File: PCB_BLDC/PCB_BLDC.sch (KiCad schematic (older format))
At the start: 70 parts, among them J1 Conn_01x01_Female, J10 Conn_01x06, J11 Conn_01x08, J12 Conn_01x06, J13 Conn_01x08, J14 Conn_01x08, J15 Conn_01x10, J16 Conn_01x08, J17 Conn_01x10, J2 Conn_01x01_Female, J3 Conn_01x01_Female, J4 Conn_01x01_Female, J5 Conn_01x01_Female, J6 Conn_01x01_Female, J7 Conn_01x01_Female, J8 VCC_Unregulated, J9 VCC_GND, Q1 IRF4905, SW1 Rotary_Encoder, U1 MagI3C WPMDH1100XX1S / 173010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, U2 BTN8962TA, U3 BTN8962TA, U4 BTN8962TA

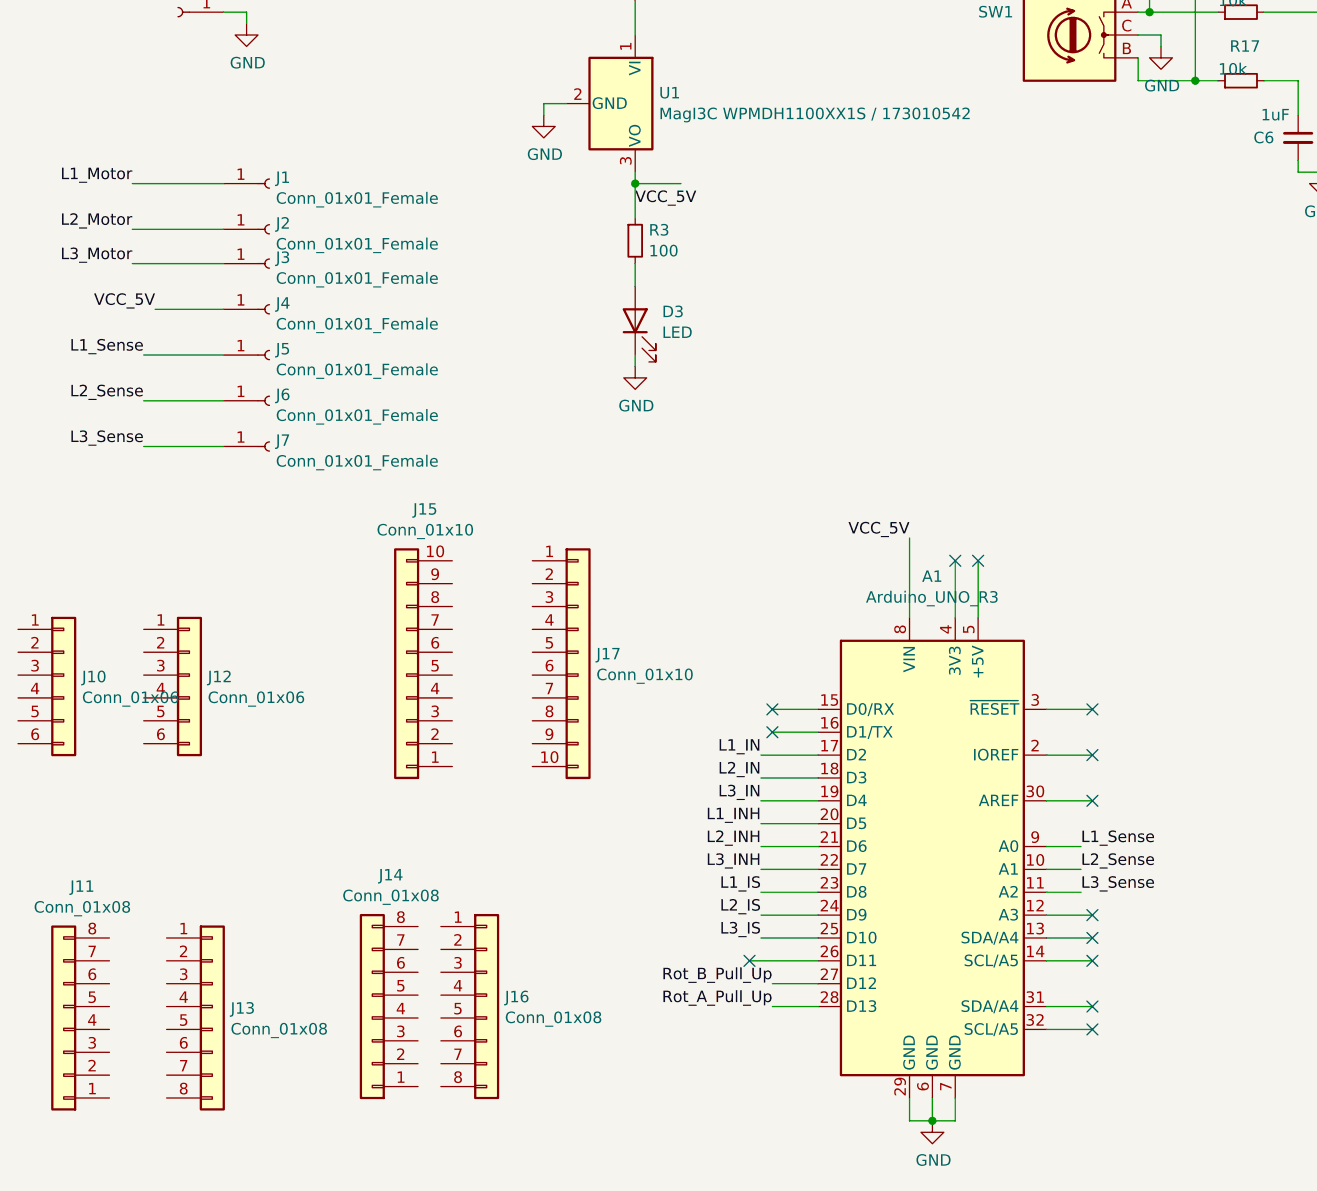
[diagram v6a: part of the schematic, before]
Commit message: Main: Update Arduino Pins, PCB Routing
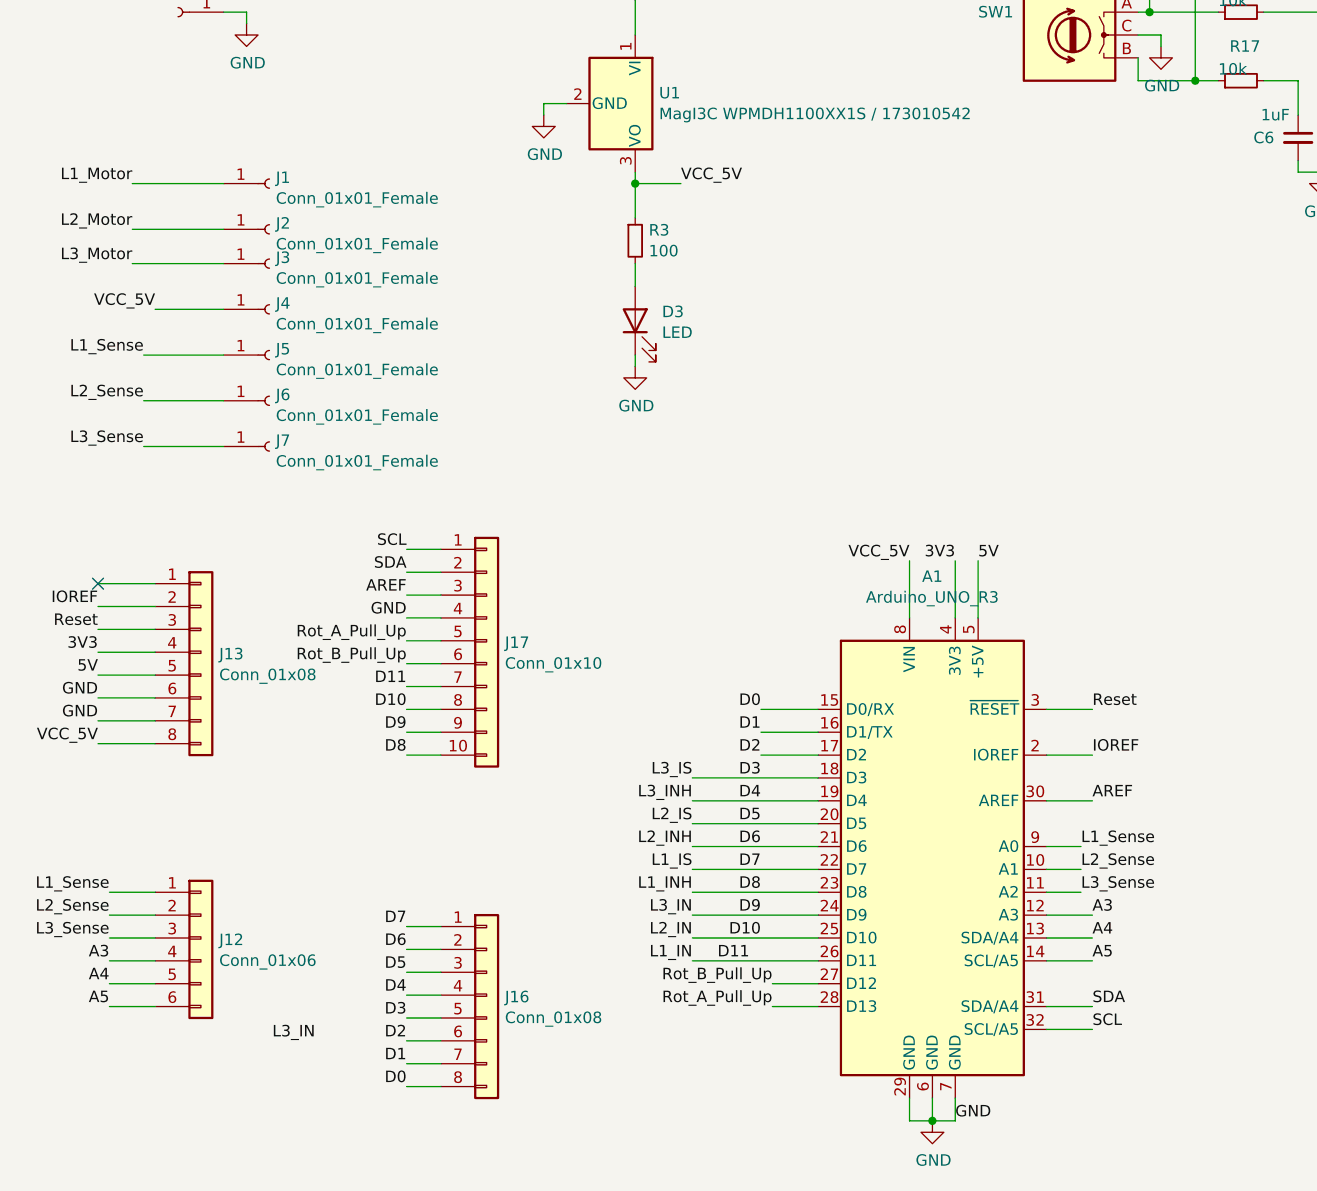
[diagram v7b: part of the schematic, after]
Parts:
- removed J10: Conn_01x06, Connector_PinHeader_2.54mm:PinHeader_1x06_P2.54mm_Vertical, symbol Connector_Generic:Conn_01x06
- removed J11, J14: Conn_01x08, Connector_PinHeader_2.54mm:PinHeader_1x08_P2.54mm_Vertical, symbol Connector_Generic:Conn_01x08
- removed J15: Conn_01x10, Connector_PinHeader_2.54mm:PinHeader_1x10_P2.54mm_Vertical, symbol Connector_Generic:Conn_01x10
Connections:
- net L2_INH is gone; now on net D6: A1.21 (D6), R11.2
- net GND: now also J13.6 (Pin_6), J13.7 (Pin_7), J17.4 (Pin_4)
- net L1_Sense: now also J12.1 (Pin_1)
- net L2_Sense: now also J12.2 (Pin_2)
- net L3_Sense: now also J12.3 (Pin_3)
- net Rot_A_Pull_Up: now also J17.5 (Pin_5)
- net Rot_B_Pull_Up: now also J17.6 (Pin_6)
- net VCC_5V: now also J13.8 (Pin_8)
- net A3: now reaches A1.12 (A3)
- net A3: now also J12.4 (Pin_4)
- net A4: now reaches A1.13 (SDA/A4)
- net A4: now also J12.5 (Pin_5)
- net A5: now reaches A1.14 (SCL/A5)
- net A5: now also J12.6 (Pin_6)
- net D0: now reaches A1.15 (D0/RX)
- net D0: now also J16.8 (Pin_8)
- net D1: now reaches A1.16 (D1/TX)
- net D1: now also J16.7 (Pin_7)
- net IOREF: now reaches A1.2 (IOREF)
- net IOREF: now also J13.2 (Pin_2)
- net D11: now reaches A1.26 (D11)
- net D11: now also J17.7 (Pin_7), R9.2
- net Reset: now reaches A1.3 (~RESET)
- net Reset: now also J13.3 (Pin_3)
- net AREF: now reaches A1.30 (AREF)
- net AREF: now also J17.3 (Pin_3)
- net SDA: now reaches A1.31 (SDA/A4)
- net SDA: now also J17.2 (Pin_2)
- net SCL: now reaches A1.32 (SCL/A5)
- net SCL: now also J17.1 (Pin_1)
- net 3V3: now reaches A1.4 (3V3)
- net 3V3: now also J13.4 (Pin_4)
- net 5V: now reaches A1.5 (+5V)
- net 5V: now also J13.5 (Pin_5)
- net D8: now reaches J17.10 (Pin_10)
- net D8: now also A1.23 (D8), R8.2
- net D10: now reaches J17.8 (Pin_8)
- net D10: now also A1.25 (D10), R12.2
- net D9: now reaches J17.9 (Pin_9)
- net D9: now also A1.24 (D9), R15.2
- net D7: now reaches J16.1 (Pin_1)
- net D7: now also A1.22 (D7), C8.1, R4.2, U2.6 (IS)
- net D6: now reaches J16.2 (Pin_2)
- net D5: now reaches J16.3 (Pin_3)
- net D5: now also A1.20 (D5), C9.1, R5.2, U3.6 (IS)
- net D4: now reaches J16.4 (Pin_4)
- net D4: now also A1.19 (D4), R14.2
- net D3: now reaches J16.5 (Pin_5)
- net D3: now also A1.18 (D3), C10.1, R6.2, U4.6 (IS)
- net D2: now reaches J16.6 (Pin_6)
- net D2: now also A1.17 (D2)
- removed net L1_IN: A1.17 (D2), R9.2
- removed net L1_INH: A1.20 (D5), R8.2
- removed net L1_IS: A1.23 (D8), C8.1, R4.2, U2.6 (IS)
- removed net L2_IN: A1.18 (D3), R12.2
- removed net L2_IS: A1.24 (D9), C9.1, R5.2, U3.6 (IS)
- removed net L3_IN: A1.19 (D4), R15.2
- removed net L3_INH: A1.22 (D7), R14.2
- removed net L3_IS: A1.25 (D10), C10.1, R6.2, U4.6 (IS)
- no-connect marks 13 -> 1
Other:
- moved on the sheet: J12, J13, J17

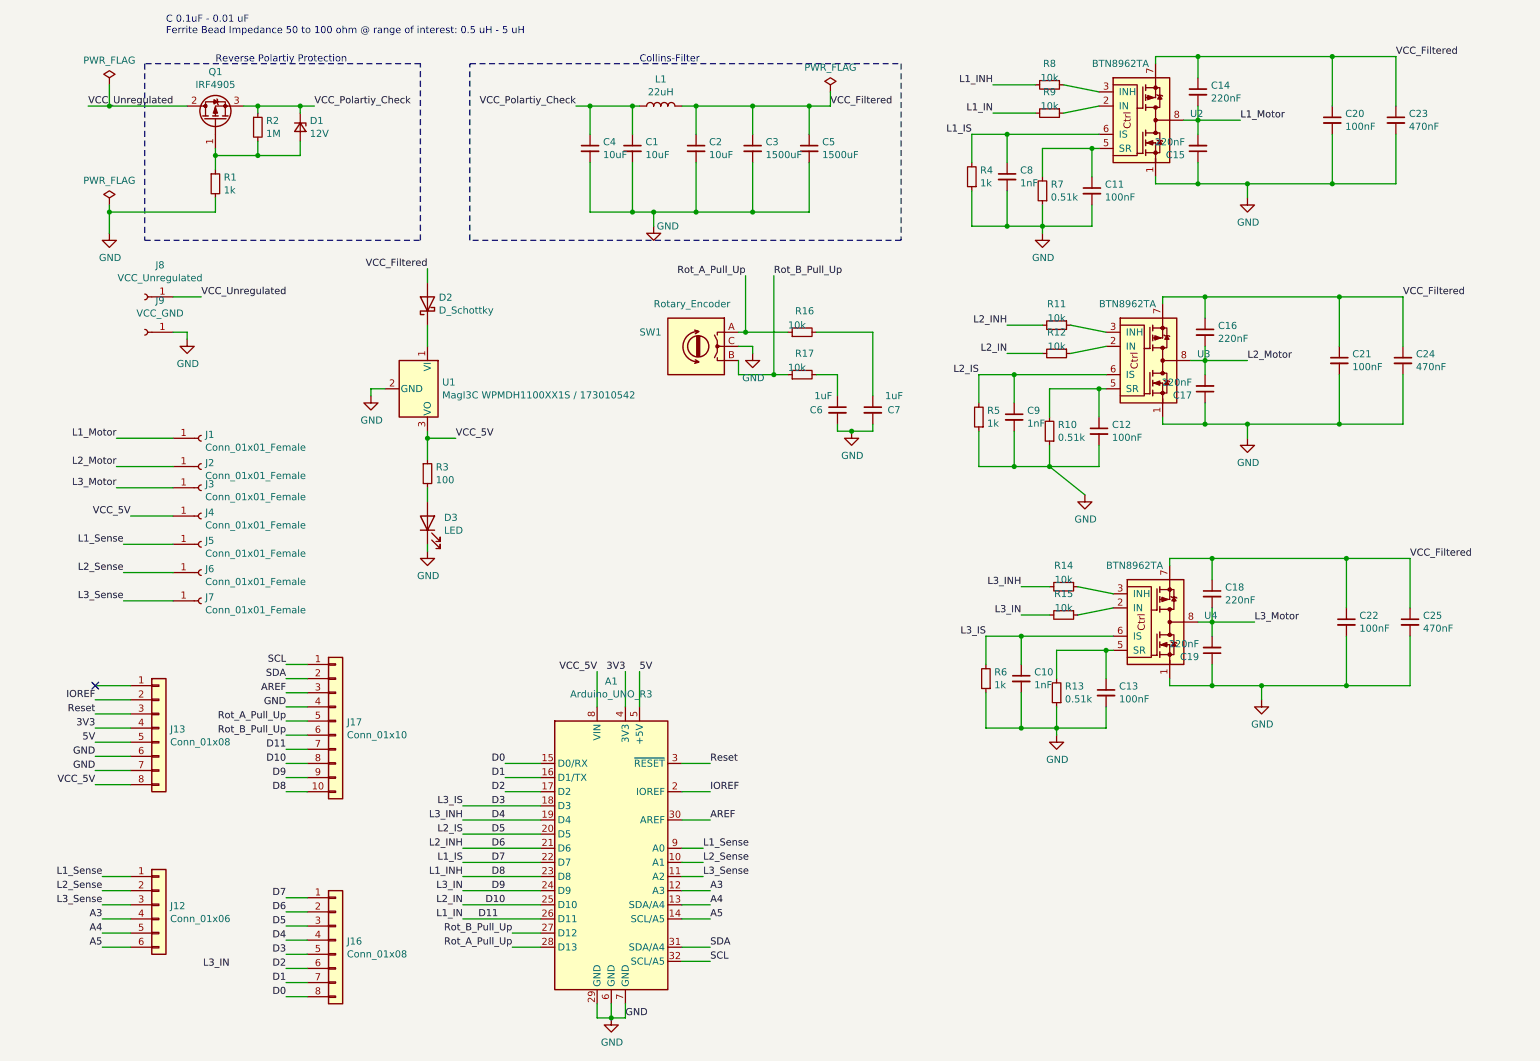
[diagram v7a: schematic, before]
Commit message: Main: Update Routing, Schmematic to use Analog Ports of Arduino
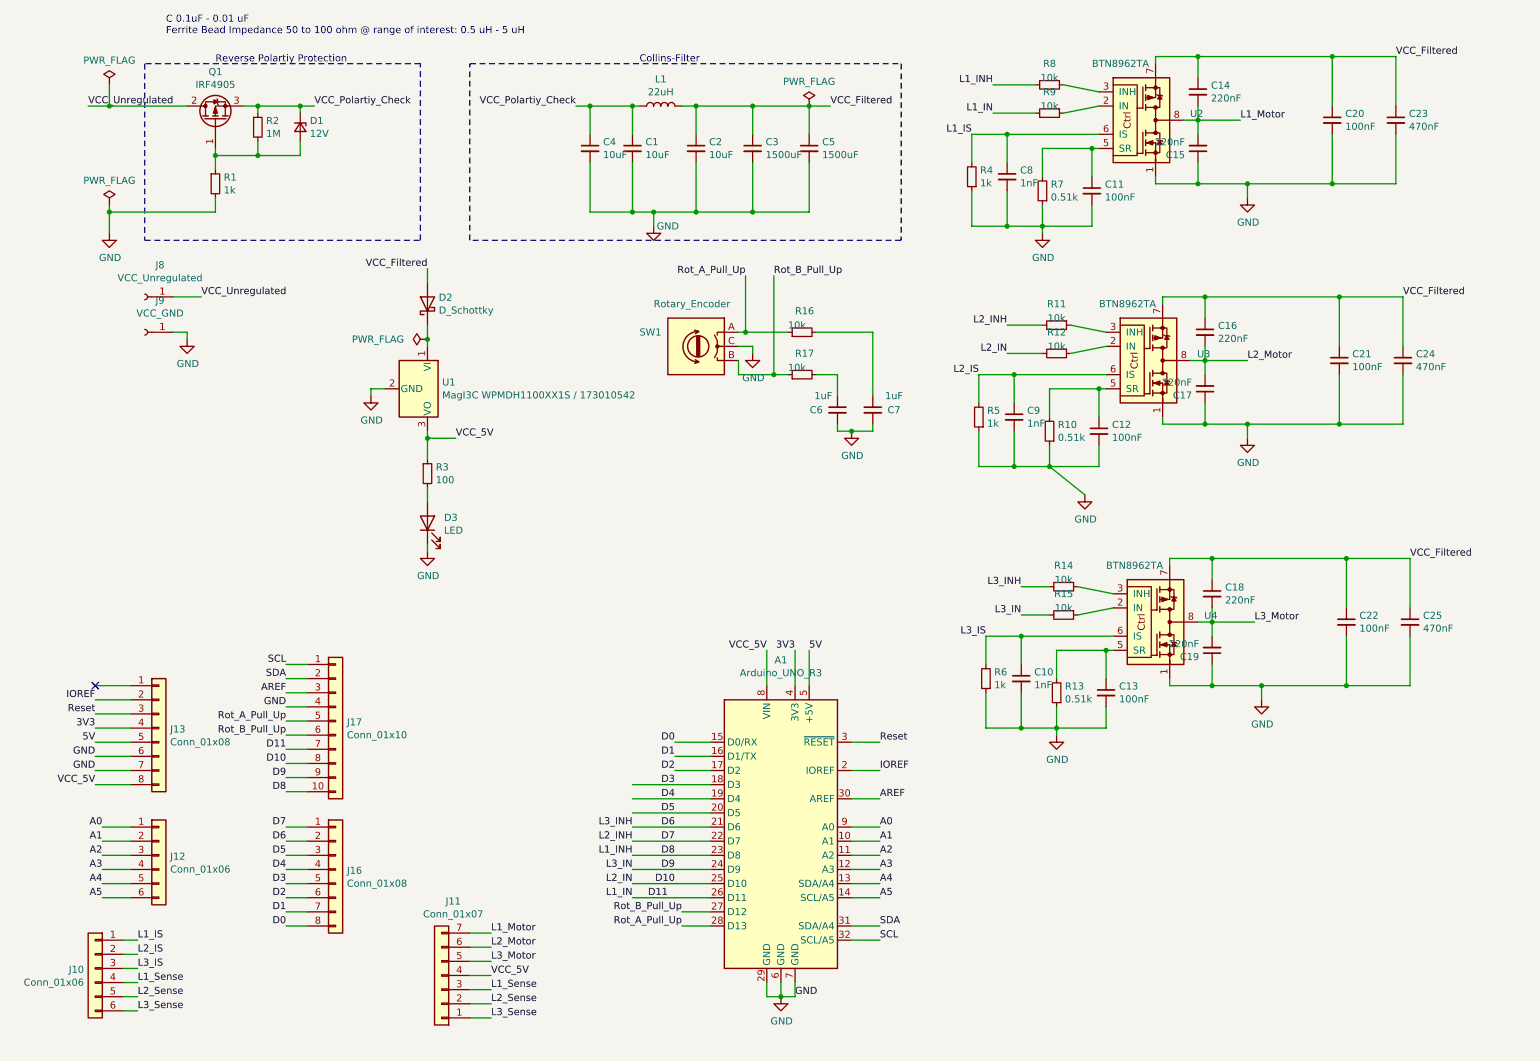
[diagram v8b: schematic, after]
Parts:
- removed J1, J2, J3, J4, J5, J6, J7: Conn_01x01_Female, Connector_Pin:Pin_D1.0mm_L10.0mm, symbol Connector:Conn_01x01_Female
- added J10: Conn_01x06, Connector_PinSocket_2.54mm:PinSocket_1x06_P2.54mm_Vertical, symbol Connector_Generic:Conn_01x06
- added J11: Conn_01x07, TerminalBlock_Phoenix:TerminalBlock_Phoenix_MKDS-1,5-7_1x07_P5.00mm_Horizontal, symbol Connector_Generic:Conn_01x07
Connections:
- net D3: no longer C10.1, R6.2, U4.6 (IS)
- net D4: no longer R14.2
- net D5: no longer C9.1, R5.2, U3.6 (IS)
- net D6: now also R14.2; no longer R11.2
- net D7: now also R11.2; no longer C8.1, R4.2, U2.6 (IS)
- net L1_Motor: now also J11.7 (Pin_7)
- net L1_Sense: now also J10.4 (Pin_4), J11.3 (Pin_3); no longer A1.9 (A0), J12.1 (Pin_1)
- net L2_Motor: now also J11.6 (Pin_6)
- net L2_Sense: now also J10.5 (Pin_5), J11.2 (Pin_2); no longer A1.10 (A1), J12.2 (Pin_2)
- net L3_Motor: now also J11.5 (Pin_5)
- net L3_Sense: now also J10.6 (Pin_6), J11.1 (Pin_1); no longer A1.11 (A2), J12.3 (Pin_3)
- net VCC_5V: now also J11.4 (Pin_4)
- new net A0: A1.9 (A0), J12.1 (Pin_1)
- new net A1: A1.10 (A1), J12.2 (Pin_2)
- new net A2: A1.11 (A2), J12.3 (Pin_3)
- new net L1_IS: C8.1, J10.1 (Pin_1), R4.2, U2.6 (IS)
- new net L2_IS: C9.1, J10.2 (Pin_2), R5.2, U3.6 (IS)
- new net L3_IS: C10.1, J10.3 (Pin_3), R6.2, U4.6 (IS)
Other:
- moved on the sheet: A1, J12, J16
